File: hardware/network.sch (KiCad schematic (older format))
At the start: 37 parts

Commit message: Almost finished layout
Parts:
- removed Y?: 25MHz, symbol Crystal_GND2
- added C14: 100n, Capacitors_SMD:C_1210, symbol C_Small
- added JP1: Shield ground, Pin_Headers:Pin_Header_Straight_1x02, symbol Jumper_NO_Small
- added X2: 25MHz, Crystals:crystal_FA238-TSX3225, symbol CRYSTAL_SMD
- C13, C18: renamed from C?; footprint (none) -> Capacitors_ThroughHole:C_Radial_D5_L11_P2
- C15, C16, C17, C19, C20, C21, C22, C26, C27, C28, C29: renamed from C?; footprint (none) -> Capacitors_SMD:C_1210
- C23: renamed from C?; value 4.7u -> 4u7; footprint (none) -> Capacitors_ThroughHole:C_Radial_D5_L11_P2
- C24, C25: renamed from C?; value 18p -> 12p; footprint (none) -> Capacitors_SMD:C_0603
- L2: renamed from L?; value Wurth 74275043 -> Wurth WE-CBF; footprint (none) -> Choke_SMD:Choke_SMD_1206_Standard
- P5: renamed from P?; footprint WIZNET_RB1-125BAG1A -> Wiznet_RJ45:WIZNET_RB1-125BAG1A
- R10, R11, R12, R13, R14, R15, R16, R17, R18, R19, R20, R21, R22, R23, R7, R8: renamed from R?; footprint (none) -> Resistors_SMD:R_1210
- R9: renamed from R?; value 12.4k/1% -> 12k4/1%; footprint (none) -> Resistors_SMD:R_1210
- gave numbers to parts that had none: 1
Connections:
- net labels added: RX+, RX-, RX1+, RX1-, RX2+, RX2-, TX+, TX-, TX1+, TX1-, ~RESET
- net labels removed: RESET
- wire segments 122 -> 128
- no-connect marks 9 -> 10
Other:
- moved on the sheet: C13, C24, C25, C26

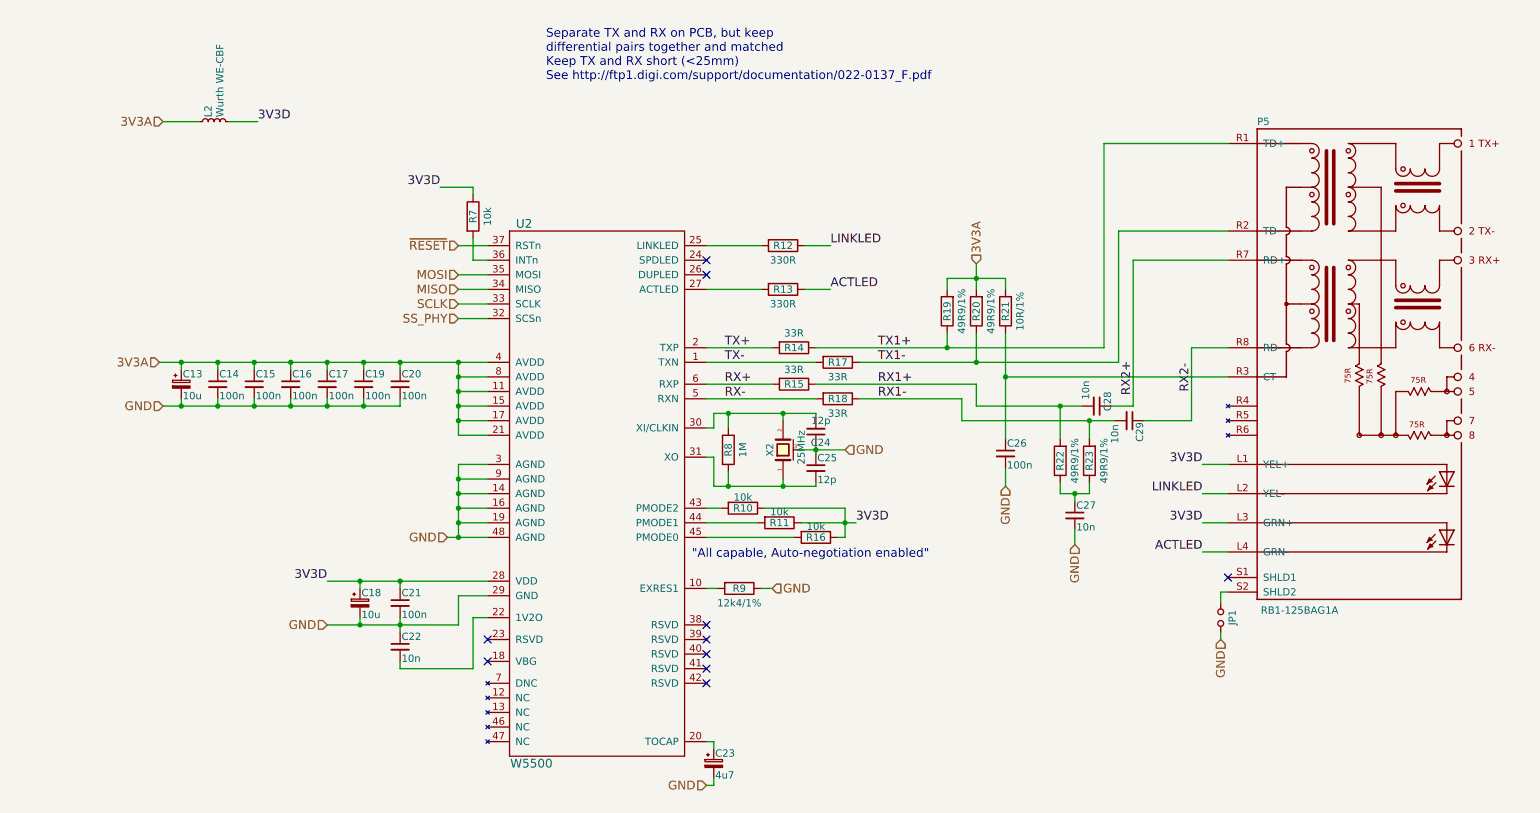
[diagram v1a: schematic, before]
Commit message: Revision of board to address issues
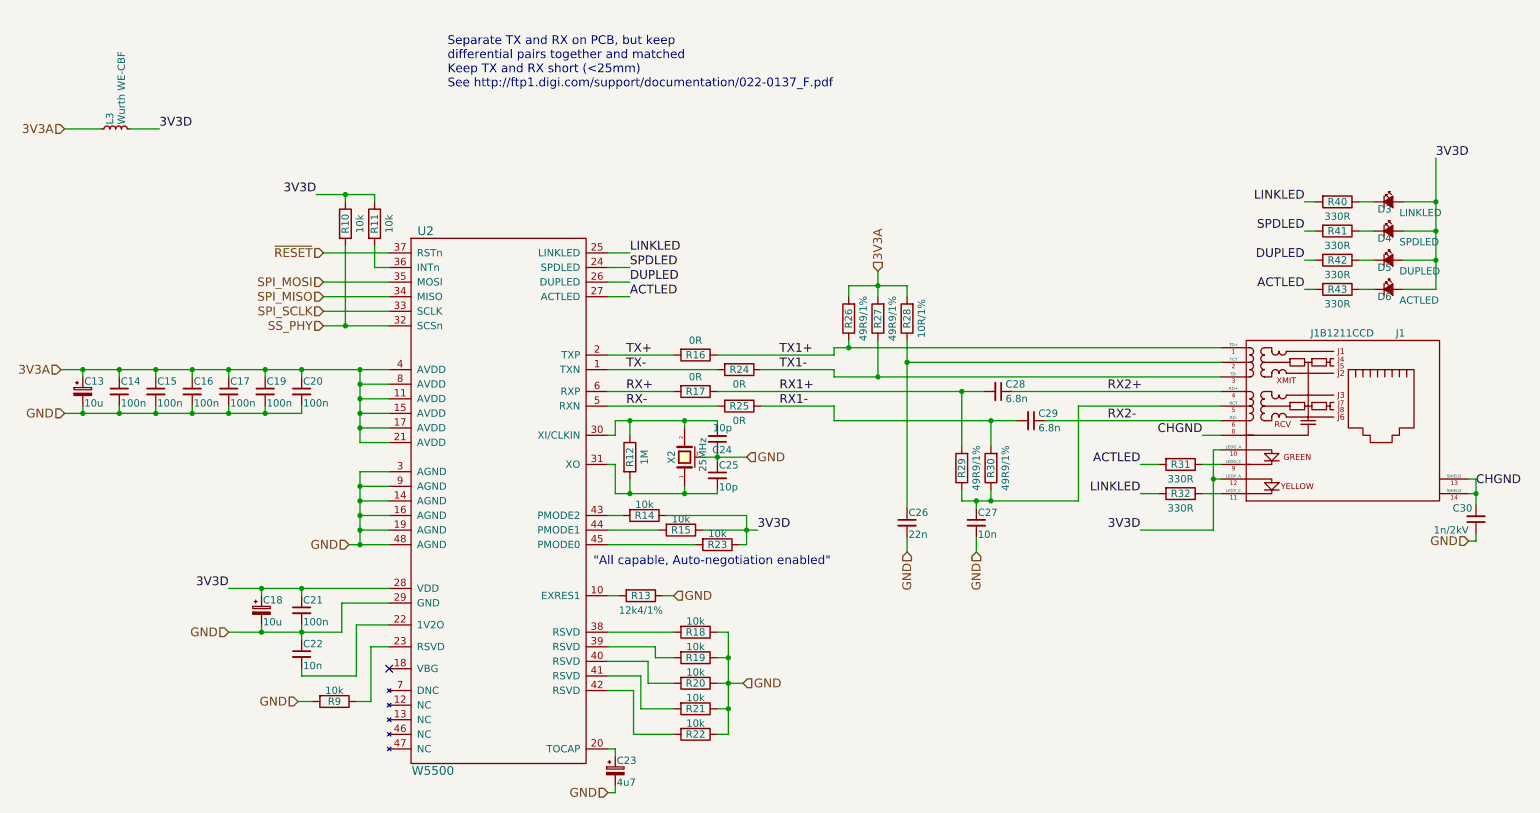
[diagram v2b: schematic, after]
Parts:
- removed JP1: Shield ground, Pin_Headers:Pin_Header_Straight_1x02, symbol Jumper_NO_Small
- removed P5: RB1-125BAG1A, Wiznet_RJ45:WIZNET_RB1-125BAG1A, symbol RB1-125BAG1A
- added C30: 1n/2kV, Capacitors_SMD:C_1206, symbol C_Small
- added D3: LINKLED, LEDs:LED_0805, symbol Led_Small
- added D4: SPDLED, LEDs:LED_0805, symbol Led_Small
- added D5: DUPLED, LEDs:LED_0805, symbol Led_Small
- added D6: ACTLED, LEDs:LED_0805, symbol Led_Small
- added J1: J1B1211CCD, Cetus_RJ45:Cetus_J1B1211CCD, symbol J1B1211CCD
- added R10, R18, R19, R20, R21, R22, R9: 10k, Resistors_SMD:R_1206, symbol R
- added R40, R41, R42, R43: 330R, Resistors_SMD:R_1206, symbol R
- C14, C15, C16, C17, C19, C20, C21, C22, C27: footprint Capacitors_SMD:C_1210 -> Capacitors_SMD:C_1206
- C24, C25: value 12p -> 10p
- C26: value 100n -> 22n; footprint Capacitors_SMD:C_1210 -> Capacitors_SMD:C_1206
- C28, C29: value 10n -> 6.8n; footprint Capacitors_SMD:C_1210 -> Capacitors_SMD:C_1206
- R11: renamed from R7; footprint Resistors_SMD:R_1210 -> Resistors_SMD:R_1206
- R12: renamed from R8; footprint Resistors_SMD:R_1210 -> Resistors_SMD:R_1206
- R13: renamed from R9; footprint Resistors_SMD:R_1210 -> Resistors_SMD:R_1206
- R14: renamed from R10; footprint Resistors_SMD:R_1210 -> Resistors_SMD:R_1206
- R15: renamed from R11; footprint Resistors_SMD:R_1210 -> Resistors_SMD:R_1206
- R16: renamed from R14; value 33R -> 0R; footprint Resistors_SMD:R_1210 -> Resistors_SMD:R_1206
- R17: renamed from R15; value 33R -> 0R; footprint Resistors_SMD:R_1210 -> Resistors_SMD:R_1206
- R23: renamed from R16; footprint Resistors_SMD:R_1210 -> Resistors_SMD:R_1206
- R24: renamed from R17; value 33R -> 0R; footprint Resistors_SMD:R_1210 -> Resistors_SMD:R_1206
- R25: renamed from R18; value 33R -> 0R; footprint Resistors_SMD:R_1210 -> Resistors_SMD:R_1206
- R26: renamed from R19; footprint Resistors_SMD:R_1210 -> Resistors_SMD:R_1206
- R27: renamed from R20; footprint Resistors_SMD:R_1210 -> Resistors_SMD:R_1206
- R28: renamed from R21; footprint Resistors_SMD:R_1210 -> Resistors_SMD:R_1206
- R29: renamed from R22; footprint Resistors_SMD:R_1210 -> Resistors_SMD:R_1206
- R30: renamed from R23; footprint Resistors_SMD:R_1210 -> Resistors_SMD:R_1206
- R31: renamed from R12; footprint Resistors_SMD:R_1210 -> Resistors_SMD:R_1206
- R32: renamed from R13; footprint Resistors_SMD:R_1210 -> Resistors_SMD:R_1206
- renumbered L2 to L3
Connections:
- net 3V3D: now also D3.2 (A), D4.2 (A), D5.2 (A), D6.2 (A), J1.10 (LEDG_A), J1.12 (LEDY_A), R10.1
- net ACTLED: now also R31.2, U2.27 (ACTLED), R43.2; no longer R32.1
- net GND: now also C30.1, R18.1, R19.1, R20.1, R21.1, R22.1, R9.2
- net LINKLED: now also R32.2, U2.25 (LINKLED), R40.2; no longer R31.1
- net RX2+: now also J1.4 (RD+)
- net RX2-: now also J1.6 (RD-)
- net SS_PHY: now also R10.2
- net TX1+: now also J1.1 (TD+)
- net TX1-: now also J1.3 (TD-)
- net at U2.23 (RSVD): now also R9.1
- net SPDLED: now reaches U2.24 (SPDLED)
- net SPDLED: now also R41.2
- net DUPLED: now reaches U2.26 (DUPLED)
- net DUPLED: now also R42.2
- net at U2.38 (RSVD): now also R18.2
- net at U2.39 (RSVD): now also R19.2
- net at U2.40 (RSVD): now also R20.2
- net at U2.41 (RSVD): now also R21.2
- net at U2.42 (RSVD): now also R22.2
- net at C26.1, R28.1: now also J1.2 (TCT)
- net at C27.1, R29.1, R30.1: now also J1.5 (RCT)
- net MISO renamed SPI_MISO
- net MOSI renamed SPI_MOSI
- net SCLK renamed SPI_SCLK
- new net: J1.11 (LEDY_C), R32.1
- new net: J1.9 (LEDG_C), R31.1
- new net: D3.1 (K), R40.1
- new net: D4.1 (K), R41.1
- new net: D5.1 (K), R42.1
- new net: D6.1 (K), R43.1
- new net CHGND: C30.2, J1.13 (SHIELD), J1.14 (SHIELD), J1.8
- no-connect marks 10 -> 1
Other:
- moved on the sheet: C13, C14, C15, C16, C17, C18, C19, C20, C21, C22, C23, C24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

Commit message: Further update to change clock package and move some components around
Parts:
- C24, C25: value 10p -> 32p
- X2: footprint Crystals:crystal_FA238-TSX3225 -> Crystals:Crystal_HC49-SD_SMD; symbol CRYSTAL_SMD -> Crystal_Small
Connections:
- net GND: no longer X2.3 (case)
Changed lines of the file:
@@
 P 5600 3875
 F 0 "C24" H 5500 3950 50  0000 L CNN
-F 1 "10p" H 5500 3800 50  0000 L CNN
+F 1 "32p" H 5500 3800 50  0000 L CNN
 F 2 "Capacitors_SMD:C_0603" H 5600 3875 50  0001 C CNN
 F 3 "" H 5600 3875 50  0000 C CNN
@@
 P 5600 4125
 F 0 "C25" H 5610 4195 50  0000 L CNN
-F 1 "10p" H 5610 4045 50  0000 L CNN
+F 1 "32p" H 5610 4045 50  0000 L CNN
 F 2 "Capacitors_SMD:C_0603" H 5600 4125 50  0001 C CNN
 F 3 "" H 5600 4125 50  0000 C CNN
@@
 GND
 $Comp
-L CRYSTAL_SMD X2
+L Crystal_Small X2
 U 1 1 5908BFB2
-P 5375 4000
-F 0 "X2" H 5375 4090 50  0000 C CNN
-F 1 "25MHz" H 5275 3875 50  0000 L CNN
-F 2 "Crystals:crystal_FA238-TSX3225" H 5375 4000 50  0001 C CNN
-F 3 "" H 5375 4000 50  0000 C CNN
-	1    5375 4000
+P 5300 4000
+F 0 "X2" H 5300 4090 50  0000 C CNN
+F 1 "25MHz" H 5200 3875 50  0000 L CNN
+F 2 "Crystals:Crystal_HC49-SD_SMD" H 5300 4000 50  0001 C CNN
+F 3 "" H 5300 4000 50  0000 C CNN
+	1    5300 4000
 	0    -1   -1   0
 $EndComp
@@
 	4900 4050 4900 4250
 Wire Wire Line
-	5475 4000 5800 4000
-Wire Wire Line
 	3150 4100 3150 4600
 Wire Wire Line
@@
 	4900 3850 4850 3850
 Wire Wire Line
-	5375 3750 5375 3800
-Wire Wire Line
-	5375 4250 5375 4200
+	5300 3750 5300 3900
+Wire Wire Line
+	5300 4250 5300 4100
 Wire Wire Line
 	4900 4250 5600 4250
@@
 Wire Wire Line
 	5600 4250 5600 4225
-Connection ~ 5375 4250
+Connection ~ 5300 4250
 Wire Wire Line
 	5600 3750 5600 3775
-Connection ~ 5375 3750
+Connection ~ 5300 3750
 Wire Wire Line
 	3050 2250 3050 2200
@@
 Wire Wire Line
 	10000 2250 10100 2250
+Wire Wire Line
+	5800 4000 5600 4000
 $EndSCHEMATC

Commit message: New revision to board
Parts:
- removed C20: 100n, Capacitors_SMD:C_1206, symbol C_Small
- removed L3: Wurth WE-CBF, Choke_SMD:Choke_SMD_1206_Standard, symbol L_Small
- removed R10, R11, R18, R19, R20, R21, R22, R9: 10k, Resistors_SMD:R_1206, symbol R
- added L1: Wurth WE-CBF, Choke_SMD:Choke_SMD_1206_Standard, symbol L_Small
- J1: footprint Cetus_RJ45:Cetus_J1B1211CCD -> Sockets_RJ45:Cetus_J1B1211CCD
- R10: renamed from R26; value 49R9/1% -> 49R9
- R11: renamed from R27; value 49R9/1% -> 49R9
- R12: renamed from R28; value 10R/1% -> 10R
- R13: renamed from R29; value 49R9/1% -> 49R9
- R14: renamed from R30; value 49R9/1% -> 49R9
- renumbered C17 to C10, C18 to C11, C19 to C12, C21 to C13, C22 to C14, C23 to C16, C24 to C17, C25 to C18, C26 to C19, C27 to C20, C28 to C21, C29 to C22, C30 to C23, C13 to C6, C14 to C7, C15 to C8, C16 to C9, D3 to D1, D4 to D2, D5 to D3, D6 to D4, R12 to R1, R31 to R15, R32 to R16, R40 to R17, R41 to R18, R42 to R19, R13 to R2, R43 to R20, R14 to R3, R15 to R4, R16 to R5, R17 to R6, R23 to R7, R24 to R8, R25 to R9, U2 to U3, X2 to X1
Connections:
- net 3V3A: now also R3.1, R4.1, R7.1, L1.2
- net 3V3D: now also L1.1; no longer R3.1, R4.1, R7.1
- net GND: now also U3.23 (RSVD), U3.38 (RSVD), U3.39 (RSVD), U3.40 (RSVD), U3.41 (RSVD), U3.42 (RSVD)
- net ~PHY_INTERRUPT: now reaches U3.36 (INTn)
- net SS_PHY renamed PHY_SS
- net ~RESET renamed ~PHY_RESET
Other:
- moved on the sheet: C11, C13, C14

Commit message: Added some part numbers to the schematic
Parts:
- D1, D2, D3, D4: MPN1 (none) -> LG R971; Manufacturer1 (none) -> Osram Opto; SKU1 (none) -> 654-5773; Vendor1 (none) -> RS
- J1: MPN1 (none) -> J1B1211CCD; Manufacturer1 (none) -> Wiznet; SKU1 (none) -> 950-J1B1211CCD; Vendor1 (none) -> Mouser
- L1: MPN1 (none) -> 7447918; Manufacturer1 (none) -> Wurth Elektronik; SKU1 (none) -> 124-1871; Vendor1 (none) -> RS
- U3: MPN1 (none) -> W5500; Manufacturer1 (none) -> Wiznet; SKU1 (none) -> 950-W5500; Vendor1 (none) -> Mouser
- X1: MPN1 (none) -> QCS25.0000F18B23R; Manufacturer1 (none) -> QANTEK; SKU1 (none) -> 814-9550; Vendor1 (none) -> RS
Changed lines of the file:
@@
 F 2 "Housings_QFP:LQFP-48_7x7mm_Pitch0.5mm" H 4100 4250 60  0001 C CNN
 F 3 "" H 4100 4250 60  0000 C CNN
+F 4 "Wiznet" H 4100 4300 60  0001 C CNN "Manufacturer1"
+F 5 "W5500" H 4100 4300 60  0001 C CNN "MPN1"
+F 6 "Mouser" H 4100 4300 60  0001 C CNN "Vendor1"
+F 7 "950-W5500" H 4100 4300 60  0001 C CNN "SKU1"
 	1    4100 4300
 	1    0    0    -1
@@
 F 2 "Crystals:Crystal_HC49-SD_SMD" H 5300 4000 50  0001 C CNN
 F 3 "" H 5300 4000 50  0000 C CNN
+F 4 "QANTEK" H 5300 4000 60  0001 C CNN "Manufacturer1"
+F 5 "QCS25.0000F18B23R" H 5300 4000 60  0001 C CNN "MPN1"
+F 6 "RS" H 5300 4000 60  0001 C CNN "Vendor1"
+F 7 "814-9550" H 5300 4000 60  0001 C CNN "SKU1"
 	1    5300 4000
 	0    -1   -1   0
@@
 F 2 "Sockets_RJ45:Cetus_J1B1211CCD" H 10150 3750 50  0001 C CNN
 F 3 "" H 10150 3750 50  0000 C CNN
+F 4 "Wiznet" H 10150 3750 60  0001 C CNN "Manufacturer1"
+F 5 "J1B1211CCD" H 10150 3750 60  0001 C CNN "MPN1"
+F 6 "Mouser" H 10150 3750 60  0001 C CNN "Vendor1"
+F 7 "950-J1B1211CCD" H 10150 3750 60  0001 C CNN "SKU1"
 	1    10150 3750
 	1    0    0    -1
@@
 	0    1    1    0
 $EndComp
-$Comp
-L Led_Small D4
-U 1 1 59489219
-P 10200 2850
-F 0 "D4" H 10125 2800 50  0000 L CNN
-F 1 "ACTLED" H 10275 2775 50  0000 L CNN
-F 2 "LEDs:LED_0805" V 10200 2850 50  0001 C CNN
-F 3 "" V 10200 2850 50  0000 C CNN
-	1    10200 2850
-	1    0    0    -1
-$EndComp
 Text Label 10525 1950 0    60   ~ 0
 3V3D
-$Comp
-L Led_Small D3
-U 1 1 5948E084
-P 10200 2650
-F 0 "D3" H 10125 2600 50  0000 L CNN
-F 1 "DUPLED" H 10275 2575 50  0000 L CNN
-F 2 "LEDs:LED_0805" V 10200 2650 50  0001 C CNN
-F 3 "" V 10200 2650 50  0000 C CNN
-	1    10200 2650
-	1    0    0    -1
-$EndComp
-$Comp
-L Led_Small D2
-U 1 1 5948E473
-P 10200 2450
-F 0 "D2" H 10125 2400 50  0000 L CNN
-F 1 "SPDLED" H 10275 2375 50  0000 L CNN
-F 2 "LEDs:LED_0805" V 10200 2450 50  0001 C CNN
-F 3 "" V 10200 2450 50  0000 C CNN
-	1    10200 2450
-	1    0    0    -1
-$EndComp
 $Comp
 L Led_Small D1
@@
 F 2 "LEDs:LED_0805" V 10200 2250 50  0001 C CNN
 F 3 "" V 10200 2250 50  0000 C CNN
+F 4 "Osram Opto" H 10200 2250 60  0001 C CNN "Manufacturer1"
+F 5 "LG R971" H 10200 2250 60  0001 C CNN "MPN1"
+F 6 "RS" H 10200 2250 60  0001 C CNN "Vendor1"
+F 7 "654-5773" H 10200 2250 60  0001 C CNN "SKU1"
 	1    10200 2250
 	1    0    0    -1
@@
 F 2 "Choke_SMD:Choke_SMD_1206_Standard" H 1575 4900 50  0001 C CNN
 F 3 "" H 1575 4900 50  0000 C CNN
+F 4 "Wurth Elektronik" V 1575 4900 60  0001 C CNN "Manufacturer1"
+F 5 "7447918" V 1575 4900 60  0001 C CNN "MPN1"
+F 6 "RS" V 1575 4900 60  0001 C CNN "Vendor1"
+F 7 "124-1871" V 1575 4900 60  0001 C CNN "SKU1"
 	1    1575 4900
 	0    1    1    0
@@
 Text Label 1900 4900 0    60   ~ 0
 3V3D
+$Comp
+L Led_Small D2
+U 1 1 59E0C1BD
+P 10200 2450
+F 0 "D2" H 10125 2400 50  0000 L CNN
+F 1 "SPDLED" H 10275 2375 50  0000 L CNN
+F 2 "LEDs:LED_0805" V 10200 2450 50  0001 C CNN
+F 3 "" V 10200 2450 50  0000 C CNN
+F 4 "Osram Opto" H 10200 2450 60  0001 C CNN "Manufacturer1"
+F 5 "LG R971" H 10200 2450 60  0001 C CNN "MPN1"
+F 6 "RS" H 10200 2450 60  0001 C CNN "Vendor1"
+F 7 "654-5773" H 10200 2450 60  0001 C CNN "SKU1"
+	1    10200 2450
+	1    0    0    -1
+$EndComp
+$Comp
+L Led_Small D3
+U 1 1 59E0C6FE
+P 10200 2650
+F 0 "D3" H 10125 2600 50  0000 L CNN
+F 1 "DUPLED" H 10275 2575 50  0000 L CNN
+F 2 "LEDs:LED_0805" V 10200 2650 50  0001 C CNN
+F 3 "" V 10200 2650 50  0000 C CNN
+F 4 "Osram Opto" H 10200 2650 60  0001 C CNN "Manufacturer1"
+F 5 "LG R971" H 10200 2650 60  0001 C CNN "MPN1"
+F 6 "RS" H 10200 2650 60  0001 C CNN "Vendor1"
+F 7 "654-5773" H 10200 2650 60  0001 C CNN "SKU1"
+	1    10200 2650
+	1    0    0    -1
+$EndComp
+$Comp
+L Led_Small D4
+U 1 1 59E0C874
+P 10200 2850
+F 0 "D4" H 10125 2800 50  0000 L CNN
+F 1 "ACTLED" H 10275 2775 50  0000 L CNN
+F 2 "LEDs:LED_0805" V 10200 2850 50  0001 C CNN
+F 3 "" V 10200 2850 50  0000 C CNN
+F 4 "Osram Opto" H 10200 2850 60  0001 C CNN "Manufacturer1"
+F 5 "LG R971" H 10200 2850 60  0001 C CNN "MPN1"
+F 6 "RS" H 10200 2850 60  0001 C CNN "Vendor1"
+F 7 "654-5773" H 10200 2850 60  0001 C CNN "SKU1"
+	1    10200 2850
+	1    0    0    -1
+$EndComp
 $EndSCHEMATC
